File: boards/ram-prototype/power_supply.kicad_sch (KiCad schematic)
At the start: 19 parts, among them J1 PCIe_8pin, U1 TPS546D24A

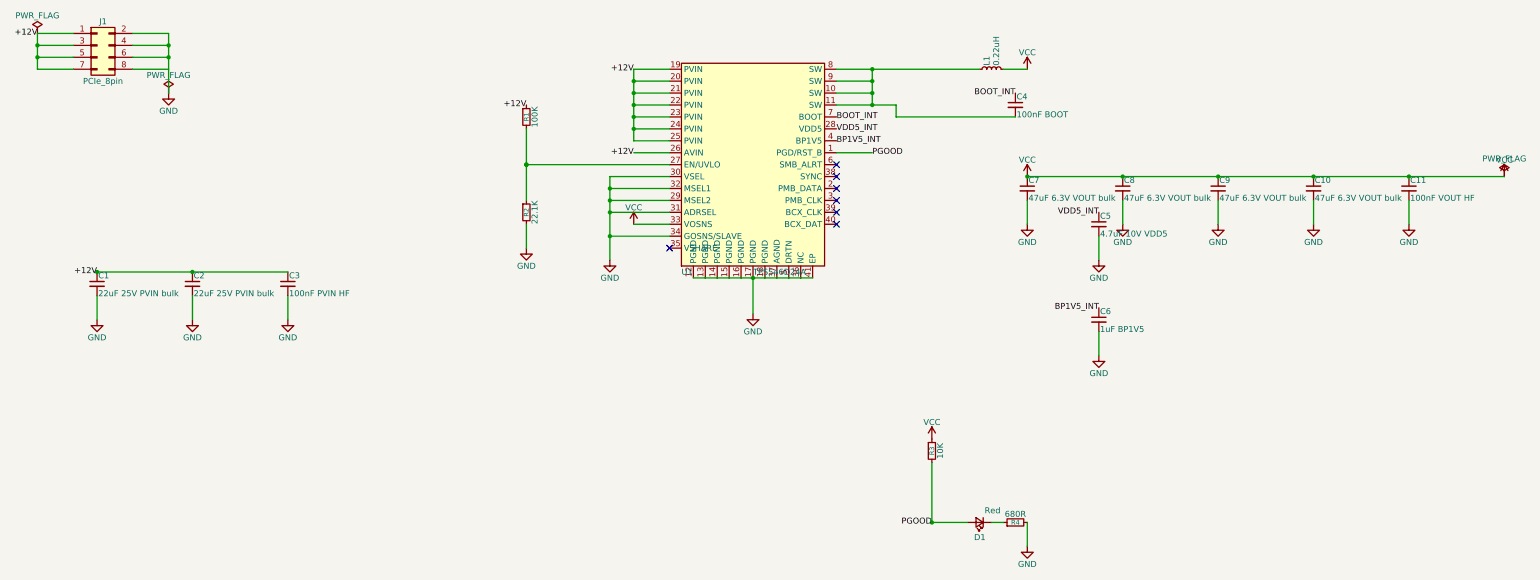
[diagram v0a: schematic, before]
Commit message: improve power supply schematic layout and symbol
- Replace BOOT_INT/VDD5_INT/BP1V5_INT labels with direct-wire horizontal
  bypass caps (angle=90) at staggered X offsets to avoid component overlap
- Replace PGOOD label + disconnected section with direct-wire pullup + LED
  at PGD pin (half-grid Y offset to avoid T-junction with boot L-route)
- Move output cap row down (16G from inductor vs 10G) for text clearance
- Remove dangling PWR_FLAG+VCC from end of output cap chain, place PWR_FLAG
  at inductor output instead
- Tighten layout: input caps 20G (was 25G), EN divider 8G (was 12G)
- TPS546D24A symbol: SW pin 8 changed to power_out (drives SW net)

Co-Authored-By: Claude Opus 4.6 (1M context) <noreply@anthropic.com>
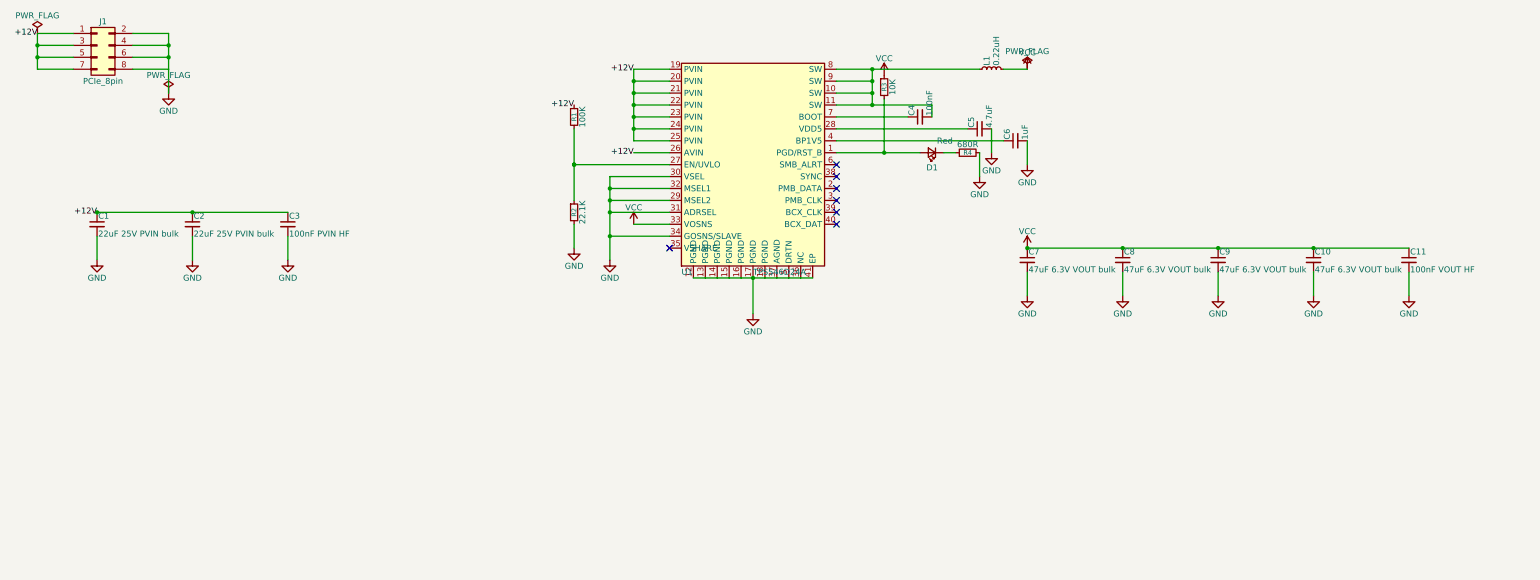
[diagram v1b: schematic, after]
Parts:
- C4: value 100nF BOOT -> 100nF
- C5: value 4.7uF 10V VDD5 -> 4.7uF
- C6: value 1uF BP1V5 -> 1uF
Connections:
- net BOOT_INT: no longer names the net of C4.1, U1.7 (BOOT)
- net BP1V5_INT: no longer names the net of C6.1, U1.4 (BP1V5)
- net PGOOD: no longer names the net of D1.2 (A), R3.2, U1.1 (PGD/RST_B)
- net VDD5_INT: no longer names the net of C5.1, U1.28 (VDD5)

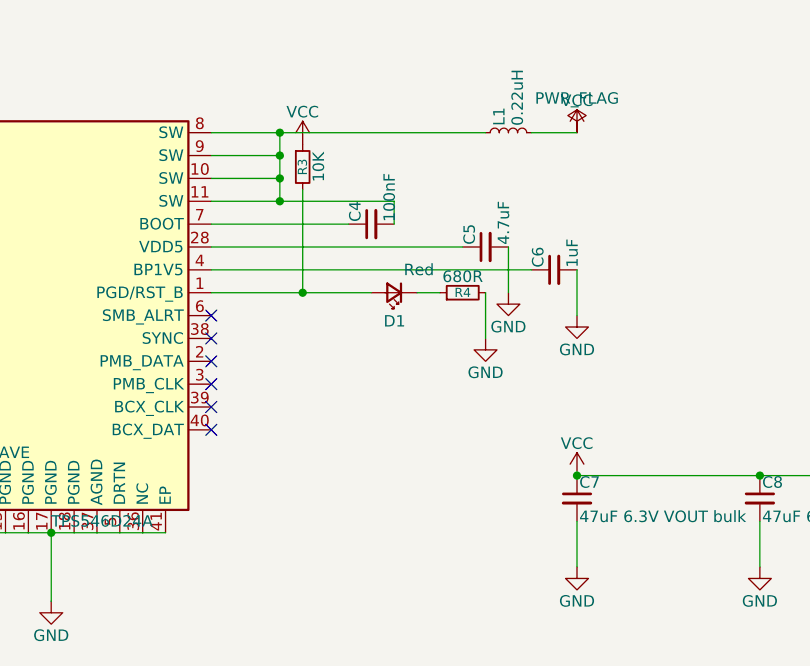
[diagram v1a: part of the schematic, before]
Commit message: add text overlap check to schematic verification and fix all violations
New check #12 in verify.py detects text overlapping wires, component
bodies, or other text. Smart exclusions for labels on their connection
wire and same-component Reference/Value pairs avoid false positives.

Fixes in generate_ram.py:
- Move ROW_SEL trunk wires from col2_x-3*GRID to col2_x-7*GRID so
  WRITE_ACTIVE/READ_EN labels don't overlap them
- Power supply: switch VDD5/BP1V5 bypass caps to angle=0 (vertical)
  with L-routes and 4*GRID vertical drop from IC pins
- Power supply: separate PGD L-route vertical X from pull-up resistor X
- Power supply: hide boot cap value (pin 2 wire unavoidably crosses it)

Co-Authored-By: Claude Opus 4.6 (1M context) <noreply@anthropic.com>
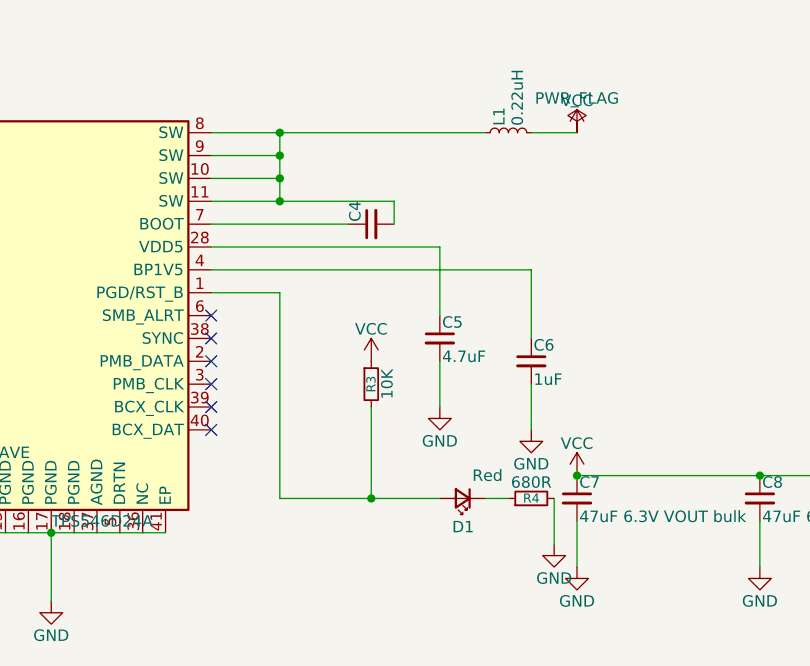
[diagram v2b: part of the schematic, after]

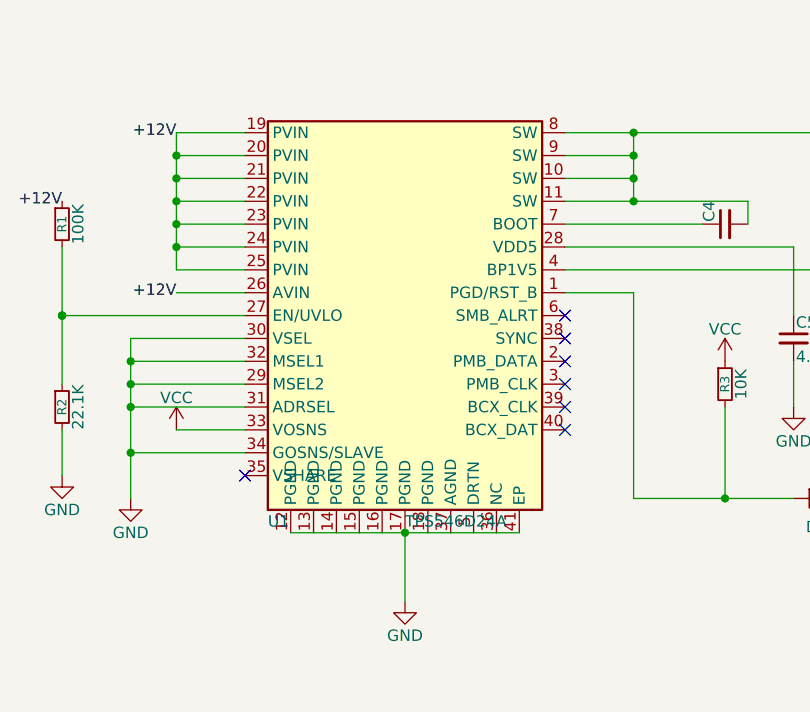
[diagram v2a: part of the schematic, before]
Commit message: expand TPS546D24A symbol corners and move ref/value to top edge
- Expand rectangle bottom from -21.59 to -26.67, top from 21.59 to 24.13
- Move all 11 bottom pins down by 5.08mm (Y -24.13 → -29.21)
- Move Reference and Value properties to top edge (Y=25.4) so bottom
  pin numbers don't cover them

Co-Authored-By: Claude Opus 4.6 (1M context) <noreply@anthropic.com>
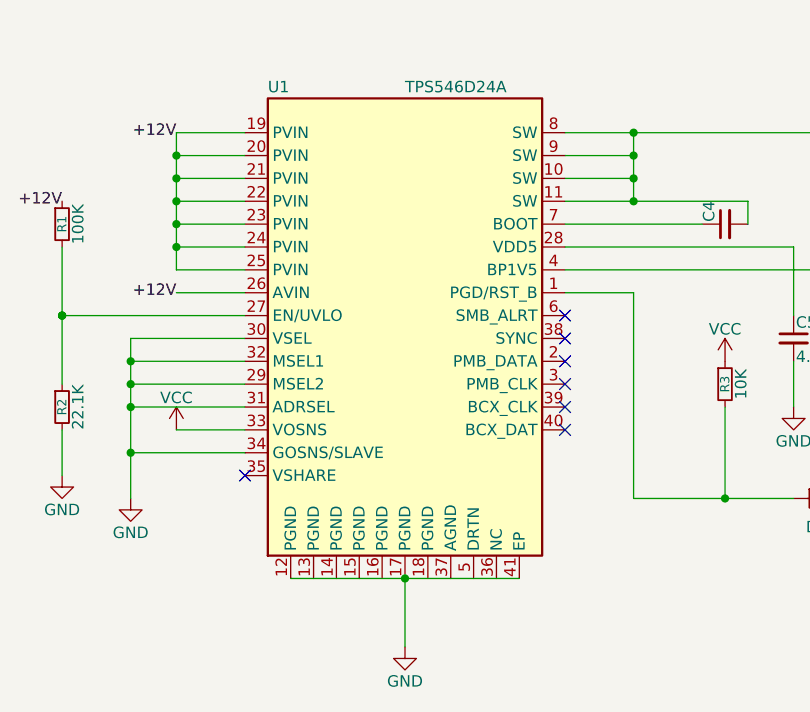
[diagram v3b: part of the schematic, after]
